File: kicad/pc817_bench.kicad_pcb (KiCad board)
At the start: 2 copper layers, 66 x 53.3 mm, 14 parts, among them J1 24V inputs, U1 PC817, U2 PC817

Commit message: Two e-stop loops: fused 24 V out to each button, return through the PC817 channel
J1 is now a 6-way terminal (24V, ES1+, ES1, ES2+, ES2, 0V) and F1 (T2A) protects
the 24 V leaving the board. Series resistors 2 x 1.5k: 6.9 mA loop current.
Board re-routed; DRC: no errors, schematic parity OK (KiCad 10.0.6).

Co-Authored-By: Claude Fable 5.1 <noreply@anthropic.com>
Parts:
- added F1: T2A, Fuse:Fuse_Littelfuse_372_D8.50mm, F.Cu at (99.0, 83.0)
- J1: value 24V inputs -> 24V + e-stops; footprint TerminalBlock_Phoenix:TerminalBlock_Phoenix_MKDS-1,5-3_1x03_P5.00mm_Horizontal -> TerminalBlock_Phoenix:TerminalBlock_Phoenix_MKDS-1,5-6_1x06_P5.00mm_Horizontal
- R1, R2, R3, R4: value 2.2k -> 1.5k
- moved J1 12.5 mm to (99.0, 91.0)
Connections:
- J1 pad 1: /IN1_24V -> Net-(J1-24V_IN)
- J1 pad 2: /IN2_24V -> /+24V
- J1 pad 3: /GND_24V -> /ES1
- R1 pad 1: /IN1_24V -> /ES1
- R3 pad 1: /IN2_24V -> /ES2
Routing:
- net /+24V: track 0.00 -> 33.2 mm
- net /IN1_24V: track 24.5 -> 0.00 mm
- net /ES1: track 0.00 -> 22.0 mm
- net /GND_24V: track 102.4 -> 84.8 mm
- net /ES2: track 0.00 -> 14.0 mm
- net /IN2_24V: track 11.5 -> 0.00 mm
- net Net-(J1-24V_IN): track 0.00 -> 8.00 mm
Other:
- board text added: "24V"
- board text added: "E-STOP INPUTS"
- board text added: "ES1"
- board text added: "ES1+"
- board text added: "ES2"
- board text added: "ES2+"
- board text removed: "IN1"
- board text removed: "PC817 24V INPUTS"

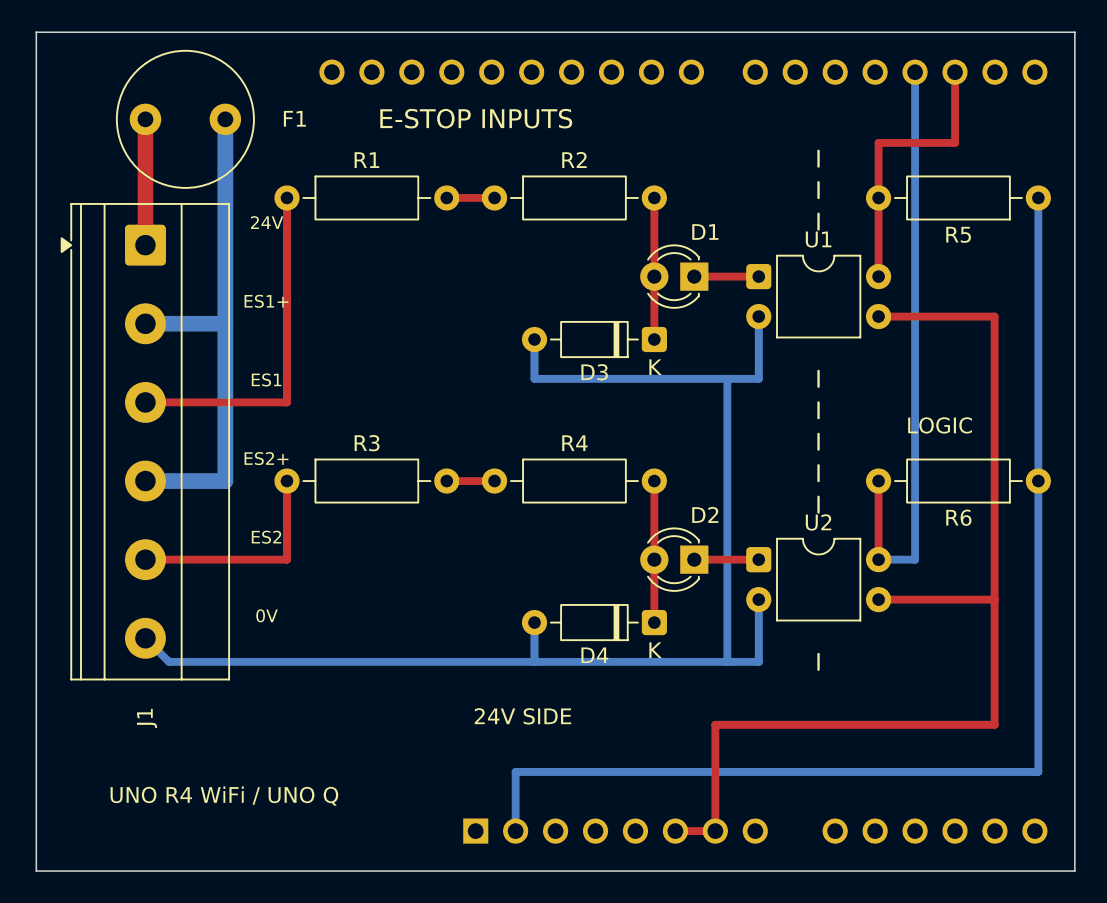
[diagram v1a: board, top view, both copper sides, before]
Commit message: Four channels: two e-stop loops (D2, D3) and two lidar inputs (D4, D5)
9-way 3.5 mm terminal, fuse on the 24 V going out to the buttons, channels at
10 mm pitch. DRC: no errors, schematic parity OK (KiCad 10.0.6).

Co-Authored-By: Claude Fable 5.1 <noreply@anthropic.com>
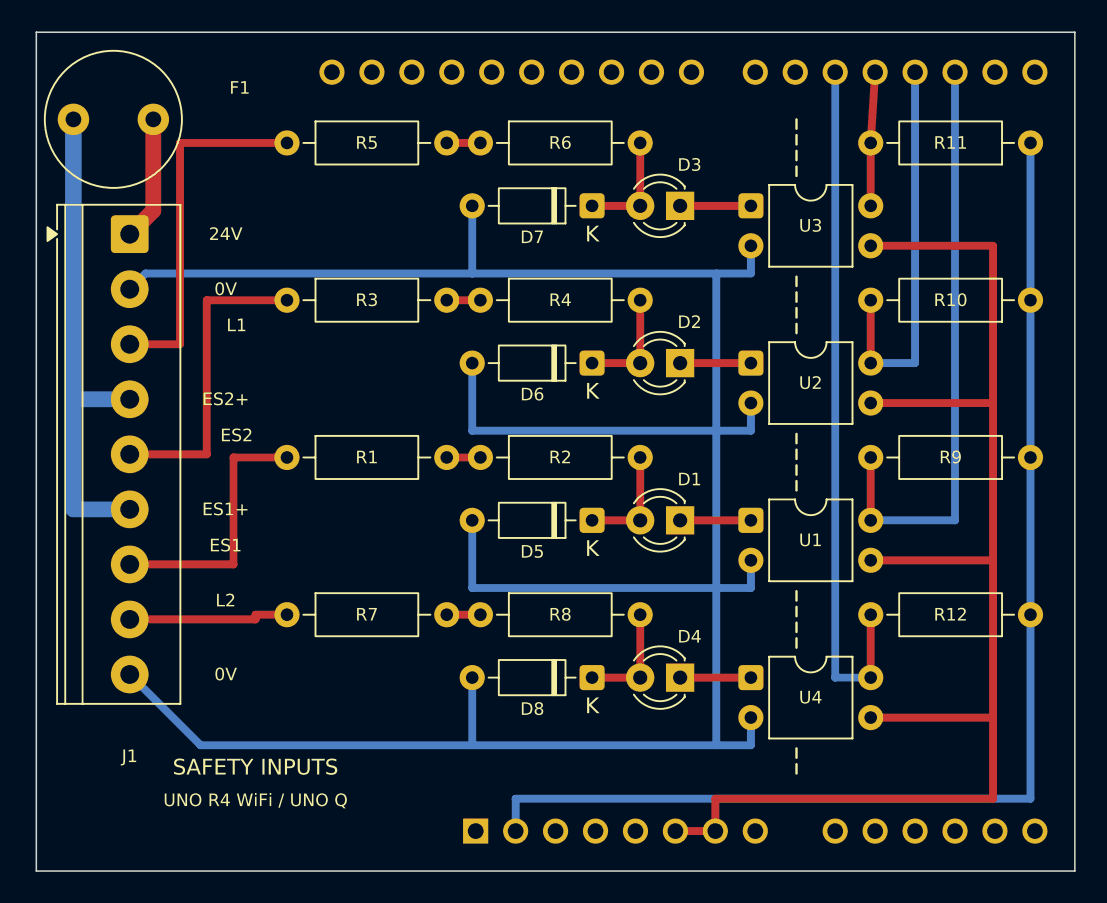
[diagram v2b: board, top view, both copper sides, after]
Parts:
- added D5: 1N4148, Diode_THT:D_DO-35_SOD27_P7.62mm_Horizontal, F.Cu at (127.4, 108.5)
- added D6: 1N4148, Diode_THT:D_DO-35_SOD27_P7.62mm_Horizontal, F.Cu at (127.4, 98.5)
- added D7: 1N4148, Diode_THT:D_DO-35_SOD27_P7.62mm_Horizontal, F.Cu at (127.4, 88.5)
- added D8: 1N4148, Diode_THT:D_DO-35_SOD27_P7.62mm_Horizontal, F.Cu at (127.4, 118.5)
- added R10: 10k, Resistor_THT:R_Axial_DIN0207_L6.3mm_D2.5mm_P10.16mm_Horizontal, F.Cu at (155.3, 94.5)
- added R11: 10k, Resistor_THT:R_Axial_DIN0207_L6.3mm_D2.5mm_P10.16mm_Horizontal, F.Cu at (155.3, 84.5)
- added R12: 10k, Resistor_THT:R_Axial_DIN0207_L6.3mm_D2.5mm_P10.16mm_Horizontal, F.Cu at (155.3, 114.5)
- added R7: 2.2k, Resistor_THT:R_Axial_DIN0207_L6.3mm_D2.5mm_P10.16mm_Horizontal, F.Cu at (108.0, 114.5)
- added R8: 2.2k, Resistor_THT:R_Axial_DIN0207_L6.3mm_D2.5mm_P10.16mm_Horizontal, F.Cu at (120.3, 114.5)
- added R9: 10k, Resistor_THT:R_Axial_DIN0207_L6.3mm_D2.5mm_P10.16mm_Horizontal, F.Cu at (155.3, 104.5)
- added U3: PC817, Package_DIP:DIP-4_W7.62mm, F.Cu at (137.5, 88.5)
- added U4: PC817, Package_DIP:DIP-4_W7.62mm, F.Cu at (137.5, 118.5)
- D3, D4: value 1N4148 -> LED red; footprint Diode_THT:D_DO-35_SOD27_P7.62mm_Horizontal -> LED_THT:LED_D3.0mm
- J1: value 24V + e-stops -> 24V, e-stops, lidars; footprint TerminalBlock_Phoenix:TerminalBlock_Phoenix_MKDS-1,5-6_1x06_P5.00mm_Horizontal -> TerminalBlock_Phoenix:TerminalBlock_Phoenix_PT-1,5-9-3.5-H_1x09_P3.50mm_Horizontal
- R5, R6: value 10k -> 2.2k
- moved R5 47.9 mm to (108.0, 84.5), turned to 0 degrees
- moved R6 41.5 mm to (120.3, 84.5), turned to 0 degrees
- moved R2 16.5 mm to (120.3, 104.5)
- moved R1 16.5 mm to (108.0, 104.5)
- moved D1 15.5 mm to (133.0, 108.5)
- moved U1 15.5 mm to (137.5, 108.5)
- moved D2 12.5 mm to (133.0, 98.5)
- moved U2 12.5 mm to (137.5, 98.5)
- moved R4 11.5 mm to (120.3, 94.5)
- moved R3 11.5 mm to (108.0, 94.5)
- moved D3 8.66 mm to (133.0, 88.5)
- moved D4 3.87 mm to (133.0, 118.5)
- moved J1 1.22 mm to (98.0, 90.3)
- moved F1 0.50 mm to (99.5, 83.0), turned to 180 degrees
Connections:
- A1 pad 19: unconnected-(A1-D4-Pad19) -> /D4
- A1 pad 20: unconnected-(A1-D5-Pad20) -> /D5
- D3 pad 1: Net-(D1-A) -> Net-(D3-K)
- D3 pad 2: /GND_24V -> Net-(D3-A)
- D4 pad 1: Net-(D2-A) -> Net-(D4-K)
- D4 pad 2: /GND_24V -> Net-(D4-A)
- J1 pad 2: /+24V -> /GND_24V
- J1 pad 3: /ES1 -> /L1
- J1 pad 6: /GND_24V -> /+24V
- R5 pad 1: /IOREF -> /L1
- R5 pad 2: /D2 -> Net-(R5-Pad2)
- R6 pad 1: /IOREF -> Net-(R5-Pad2)
- R6 pad 2: /D3 -> Net-(D3-A)
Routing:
- net /GND_24V: track 84.8 -> 171.0 mm
- net /D5: track 0.00 -> 44.8 mm
- net /L1: track 0.00 -> 22.8 mm
- net /GND: track 67.8 -> 88.5 mm
- net /D2: track 17.9 -> 37.9 mm
- net /+24V: track 33.2 -> 49.8 mm
- net /D3: track 38.3 -> 25.3 mm
- net /L2: track 0.00 -> 10.3 mm
- net /D4: track 0.00 -> 8.51 mm
- net Net-(D4-A): track 0.00 -> 7.06 mm
- net Net-(D3-A): track 0.00 -> 7.06 mm
- net /ES2: track 14.0 -> 19.8 mm
- net /ES1: track 22.0 -> 16.8 mm
- net Net-(D4-K): track 0.00 -> 4.50 mm
- net Net-(D3-K): track 0.00 -> 4.50 mm
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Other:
- board text added: "L1"
- board text added: "L2"
- board text added: "SAFETY INPUTS"
- board text removed: "24V SIDE"
- board text removed: "E-STOP INPUTS"
- board text removed: "LOGIC"

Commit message: Proto-shield variant in KiCad: grid footprints, 8-way terminal, board file models the build plan
Solder bridges and bare-wire runs are solder-side tracks; insulated wires stay
as ratsnest. check.sh verifies parity with the schematic and the wire count.
Plan reworked for physical clearances (diode away from the LED, fuse clear of
the header and terminal): 16 x 16 pads.

Co-Authored-By: Claude Fable 5.1 <noreply@anthropic.com>
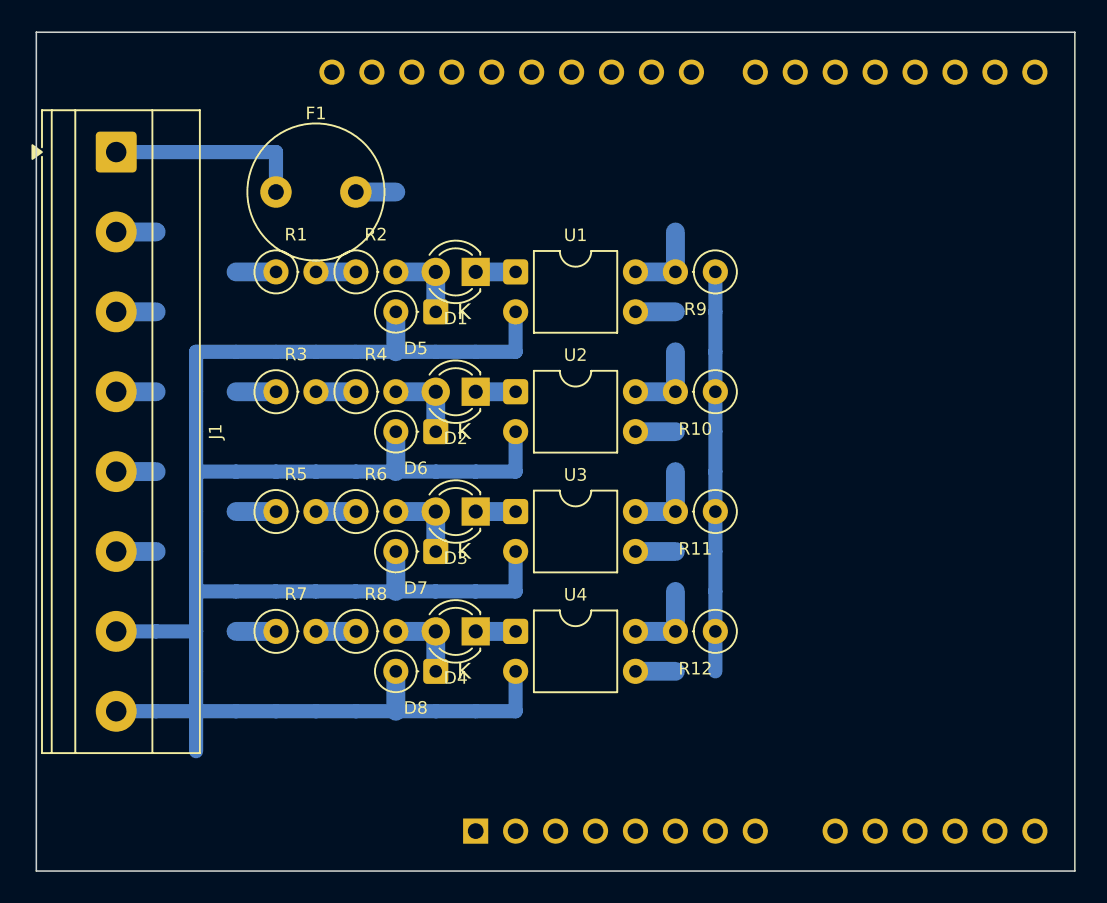
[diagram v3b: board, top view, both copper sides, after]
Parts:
- D5, D6, D7, D8: footprint Diode_THT:D_DO-35_SOD27_P7.62mm_Horizontal -> Diode_THT:D_DO-35_SOD27_P2.54mm_Vertical_CathodeUp
- J1: footprint TerminalBlock_Phoenix:TerminalBlock_Phoenix_PT-1,5-9-3.5-H_1x09_P3.50mm_Horizontal -> TerminalBlock_Phoenix:TerminalBlock_Phoenix_MKDS-1,5-8-5.08_1x08_P5.08mm_Horizontal
- R1, R10, R11, R12, R2, R3, R4, R5, R6, R7, R8, R9: footprint Resistor_THT:R_Axial_DIN0207_L6.3mm_D2.5mm_P10.16mm_Horizontal -> Resistor_THT:R_Axial_DIN0207_L6.3mm_D2.5mm_P2.54mm_Vertical
- moved R11 30.8 mm to (135.2, 107.9)
- moved R6 24.7 mm to (112.4, 107.9)
- moved U3 24.5 mm to (122.5, 107.9)
- moved D7 24.1 mm to (117.5, 110.5)
- moved R5 23.5 mm to (107.3, 107.9)
- moved D3 23.4 mm to (120.0, 107.9)
- moved R9 23.3 mm to (135.2, 92.7)
- moved U1 21.8 mm to (122.5, 92.7)
- moved R10 20.9 mm to (135.2, 100.3)
- moved D1 20.5 mm to (120.0, 92.7)
- moved R12 20.1 mm to (135.2, 115.6)
- moved D5 16.6 mm to (117.5, 95.2)
- moved U4 15.2 mm to (122.5, 115.6)
- moved U2 15.1 mm to (122.5, 100.3)
- moved R2 14.2 mm to (112.4, 92.7)
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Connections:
- J1 pad 2: /GND_24V -> /+24V
- J1 pad 3: /L1 -> /ES1
- J1 pad 4: /+24V -> /ES2
- J1 pad 5: /ES2 -> /L1
- J1 pad 6: /+24V -> /L2
- J1 pad 7: /ES1 -> /GND_24V
- J1 pad 8: /L2 -> /GND_24V
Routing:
- net /GND: track 88.5 -> 10.2 mm
- net /IOREF: track 76.5 -> 25.4 mm
- net /+24V: track 49.8 -> 5.08 mm
- net /D5: track 44.8 -> 5.08 mm
- net /GND_24V: track 171.0 -> 137.2 mm
- net /D2: track 37.9 -> 5.08 mm
- net /D3: track 25.3 -> 5.08 mm
- net /L1: track 22.8 -> 5.08 mm
- net /ES2: track 19.8 -> 5.08 mm
- net /ES1: track 16.8 -> 5.08 mm
- net /L2: track 10.3 -> 5.08 mm
- net Net-(J1-24V_IN): track 7.92 -> 12.7 mm
- net /D4: track 8.51 -> 5.08 mm
- net Net-(D3-A): track 7.06 -> 5.08 mm
- net Net-(D4-A): track 7.06 -> 5.08 mm
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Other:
- board text added: "0"
- board text added: "1"
- board text added: "10"
- board text added: "11"
- board text added: "12"
- board text added: "13"
- board text added: "14"
- board text added: "15"
- board text added: "2"
- board text added: "3"
- board text added: "4"
- board text added: "5"
- board text added: "6"
- board text added: "7"
- board text added: "8"
- board text added: "9"
- board text added: "Cmts.User lines = insulated wires"
- board text removed: "0V"
- board text removed: "24V"
- board text removed: "ES1"
- board text removed: "ES1+"
- board text removed: "ES2"
- board text removed: "ES2+"
- board text removed: "L1"
- board text removed: "L2"
- board text removed: "SAFETY INPUTS"
- board text removed: "UNO R4 WiFi / UNO Q"
